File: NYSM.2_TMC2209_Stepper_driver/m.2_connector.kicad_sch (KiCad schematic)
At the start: 1 part, among them U2 M.2-B-KEY

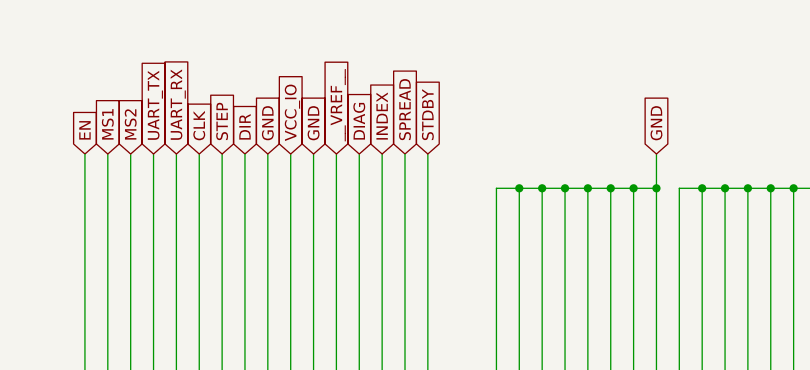
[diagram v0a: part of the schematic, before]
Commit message: Preliminary push for alternative version with External Sense Resistors
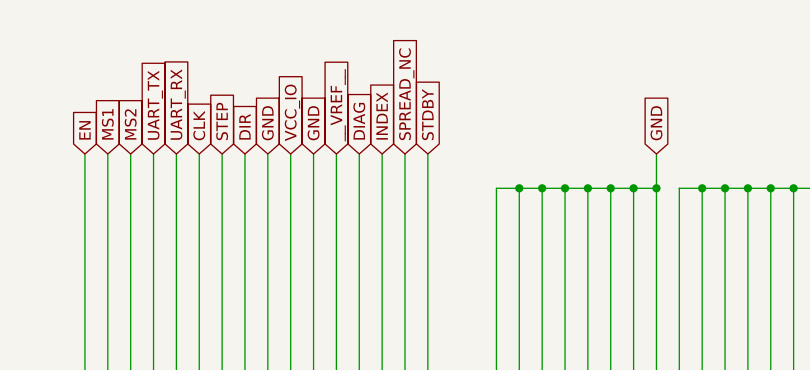
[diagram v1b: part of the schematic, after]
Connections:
- net SPREAD renamed SPREAD_NC
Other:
- title: NYSM.2 TMC2209 Module -> NYSM.2 TMC2209 Module with External Sense Resistors
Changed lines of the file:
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@@
 	(paper "A4")
 	(title_block
-		(title "NYSM.2 TMC2209 Module")
-		(date "2024-10-22")
-		(rev "2")
+		(title "NYSM.2 TMC2209 Module with External Sense Resistors")
+		(date "2024-11-08")
+		(rev "3")
 		(company "Boltz R&D")
 		(comment 1 "License: This work is licensed under GPLV3")
@@
 		)
 	)
-	(global_label "SPREAD"
+	(global_label "SPREAD_NC"
 		(shape input)
 		(at 135.89 52.07 90)
@@
 		)
 		(property "Intersheetrefs" "${INTERSHEET_REFS}"
-			(at 135.89 41.8277 90)
-			(effects
-				(font
+			(at 135.89 38.2596 90)
+			(effects
+				(font
